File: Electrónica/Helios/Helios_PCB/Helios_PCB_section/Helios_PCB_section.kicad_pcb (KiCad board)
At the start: 2 copper layers, 38 x 38 mm, 9 parts, among them J1 Conn_01x02_Socket, J2 Conn_01x02_Socket, J3 Conn_01x02_Socket, J4 Conn_01x04_Pin, J5 Conn_01x04_Pin, J6 Conn_01x04_Pin, U1 Sparkfun_Pro_Micro

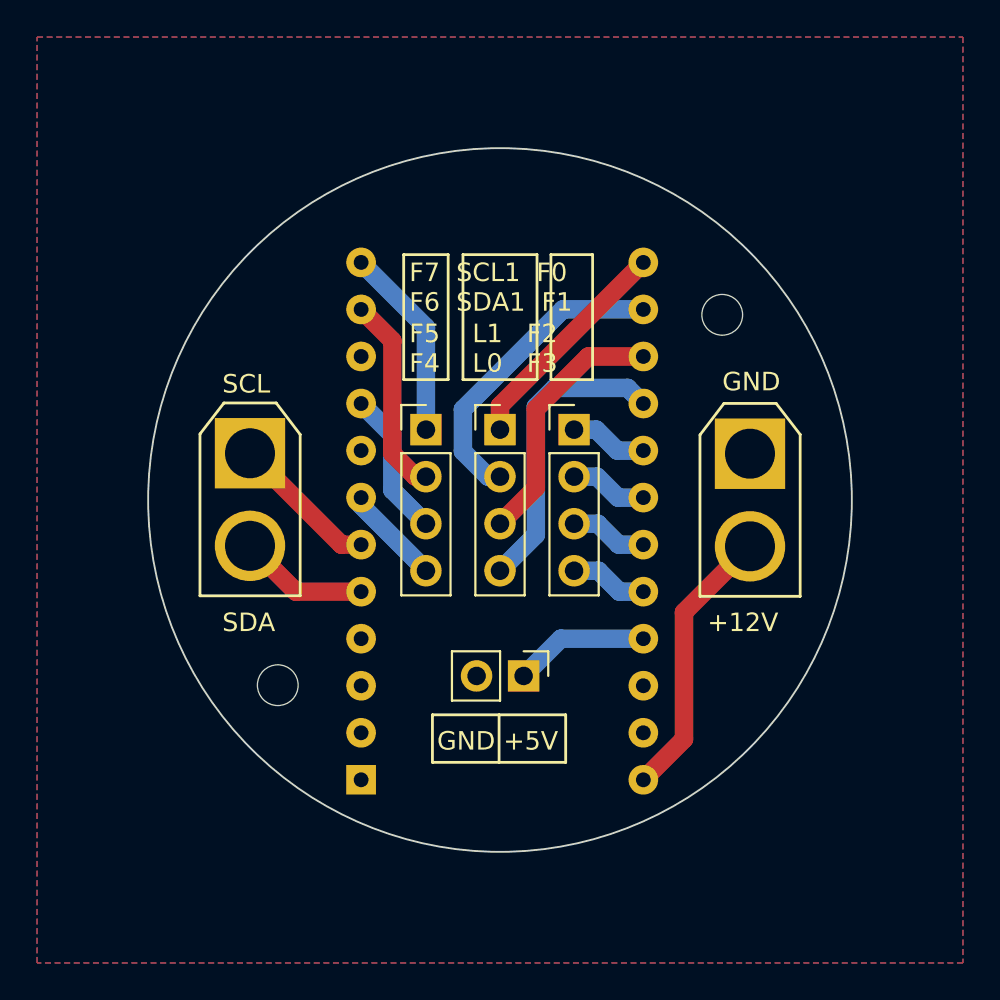
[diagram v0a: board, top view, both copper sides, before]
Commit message: Added IMU PCB, female connection 3d model, assemblies. Error detected: invert connectors in PCB Male
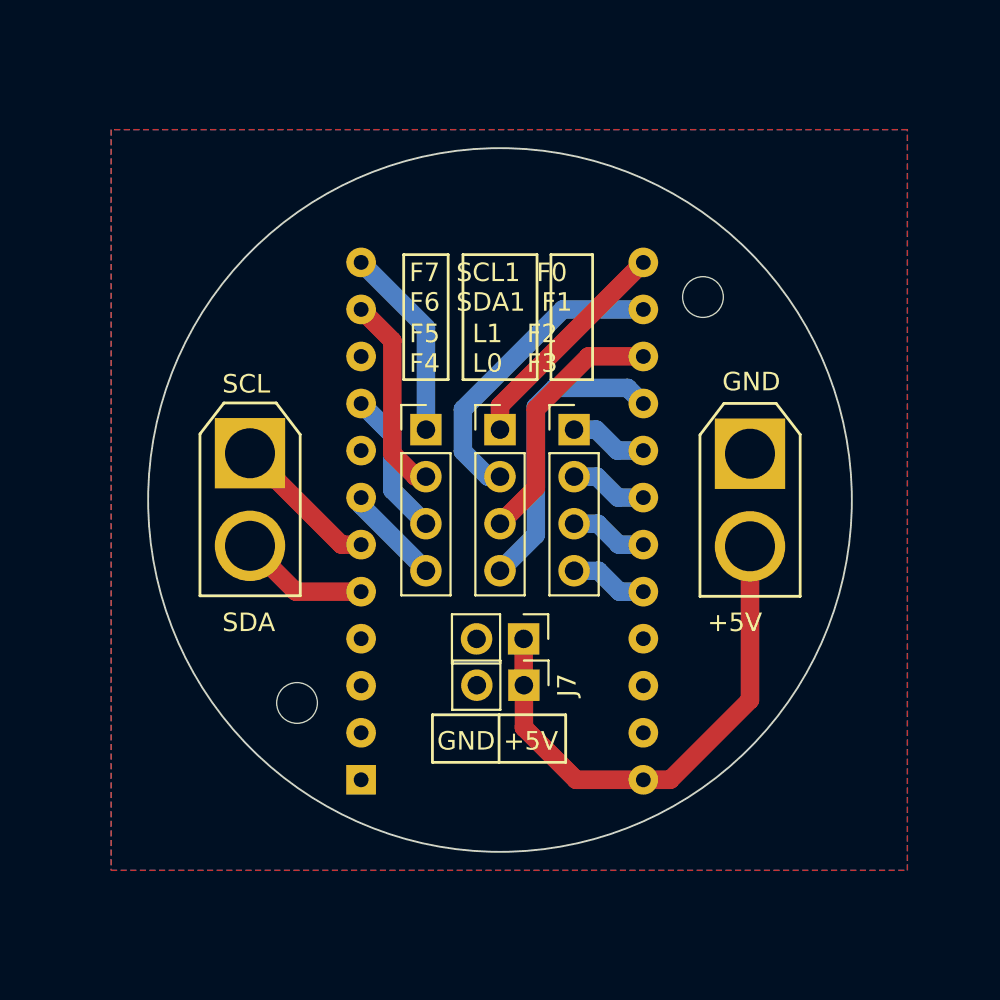
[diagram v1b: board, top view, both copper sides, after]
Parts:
- added J7: Conn_01x02_Socket, Connector_PinHeader_2.54mm:PinHeader_1x02_P2.54mm_Vertical, F.Cu at (106.3, 100.0)
- moved J2 2.00 mm to (106.3, 97.5)
- moved H1 1.42 mm to (94.0, 101.0)
- moved H2 1.42 mm to (116.0, 79.0)
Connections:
- J1 pad 2: +12V -> +5V
- U1 pad 21: +5V -> unconnected-(U1-VCC-Pad21)
- U1 pad 24: +12V -> +5V
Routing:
- net +5V: track 7.30 -> 28.3 mm
- net +12V: track 15.0 -> 0.00 mm
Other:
- board text added: "+5V"
- board text removed: "+12V"

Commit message: Helios Panel
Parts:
- added G***: LOGO, LOGO, B.Cu at (118.9, 81.9)
- added G***: LOGO, LOGO, B.Cu at (117.4, 98.2)
- added G***: LOGO, LOGO, B.Cu at (105.0, 72.2)
- added G***: LOGO, LOGO, B.Cu at (90.6, 97.9)
- added G***: LOGO, LOGO, B.Cu at (92.7, 81.0)
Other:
- board text added: "5V"
- board text added: "Colabora:"
- board text added: "Helios V2.1 2023"
- board text added: "JaimeBravoAlgaba Helios_SoftRobot"
- board text added: "SCL"
- board text added: "SDA"
- board text removed: "+5V"
- board text removed: "SCL SDA"
